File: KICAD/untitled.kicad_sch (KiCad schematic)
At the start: 73 parts, among them IC1 TPA3116D2QDADRQ1, IC2 TPA3116D2QDADRQ1

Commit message: clear
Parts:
- IC1, IC2: footprint TPA3116D2QDADRQ1:SOP65P810X120-33N -> footprints:TPA3116D2QDADRQ1
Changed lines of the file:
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@@
 			)
 		)
-		(property "Footprint" "TPA3116D2QDADRQ1:SOP65P810X120-33N"
+		(property "Footprint" "footprints:TPA3116D2QDADRQ1"
 			(at 177.8 157.15 0)
 			(hide yes)
@@
 			)
 		)
-		(property "Footprint" "TPA3116D2QDADRQ1:SOP65P810X120-33N"
+		(property "Footprint" "footprints:TPA3116D2QDADRQ1"
 			(at 177.8 244.78 0)
 			(hide yes)

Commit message: tiens mec
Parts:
- added R28, R33: 12k, symbol Device:R_Small
- added R32, R34: 13k, symbol Device:R_Small
- added U5, U6: LM321, Package_TO_SOT_SMD:SOT-23-5, symbol Amplifier_Operational:LM321
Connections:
- net GND: now also R28.1, R33.1, U5.2 (V-), U6.2 (V-)
- net at C8.2, IC1.7 (GVDD), R3.1: no longer IC1.6 (PLIMIT)
- net at C30.2, IC2.7 (GVDD), R10.1: no longer IC2.6 (PLIMIT)
- new net: R33.2, R34.2, U6.3 (-)
- new net: R28.2, R32.2, U5.3 (-)
- new net +20V: U5.5 (V+), U6.5 (V+)
- new net AOP_STEREO: U5.1 (+)
- new net AOP_SUB: U6.1 (+)
- new net PLIMIT_STEREO: IC1.6 (PLIMIT), R32.1, U5.4
- new net PLIMIT_SUB: IC2.6 (PLIMIT), R34.1, U6.4

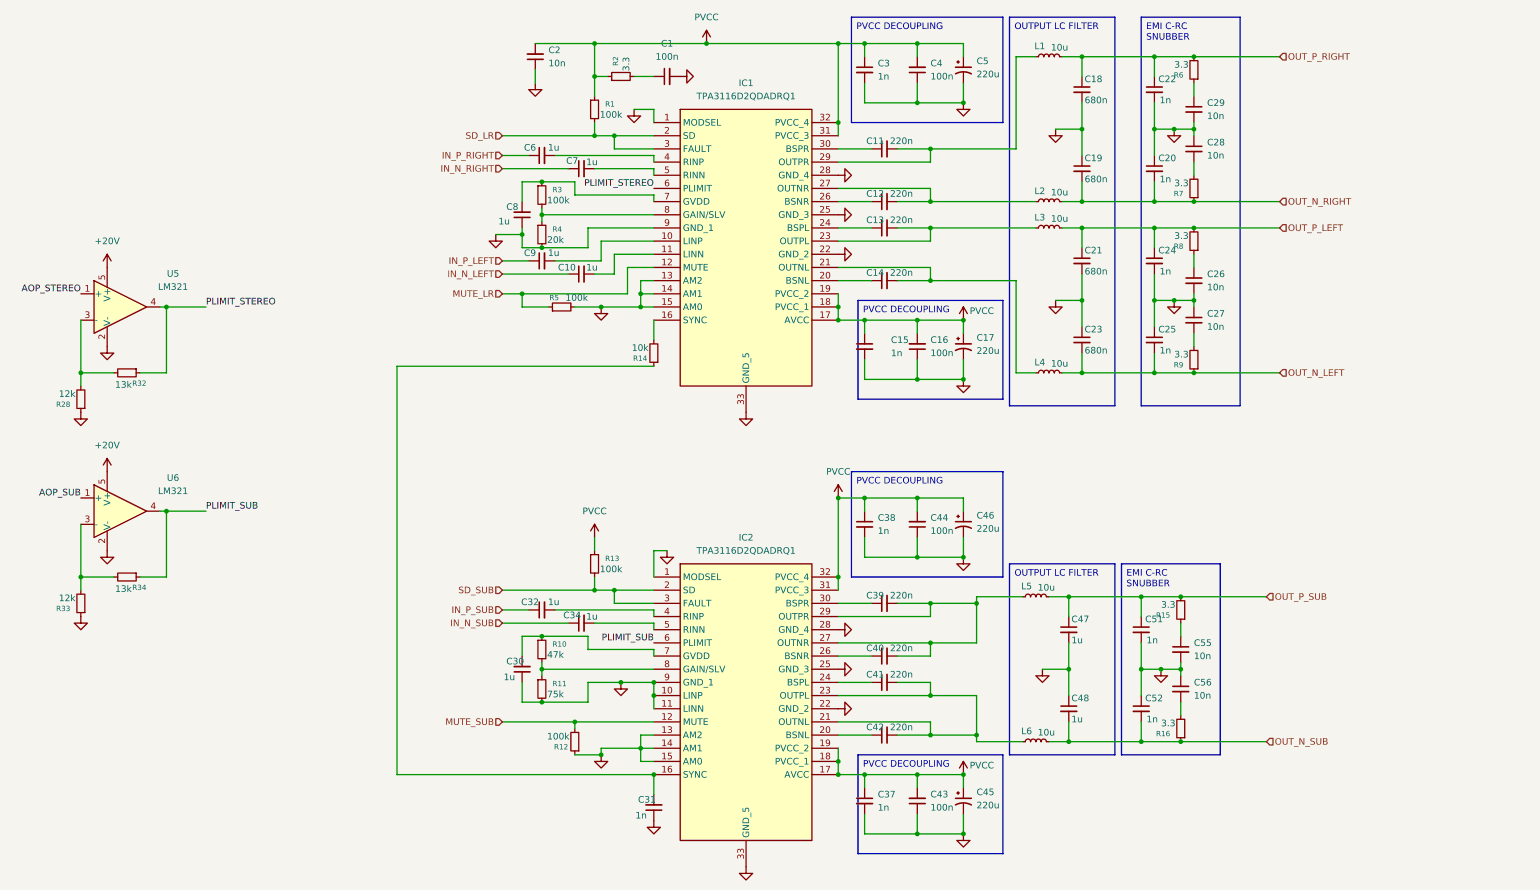
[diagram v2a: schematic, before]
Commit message: supression du subwoofer
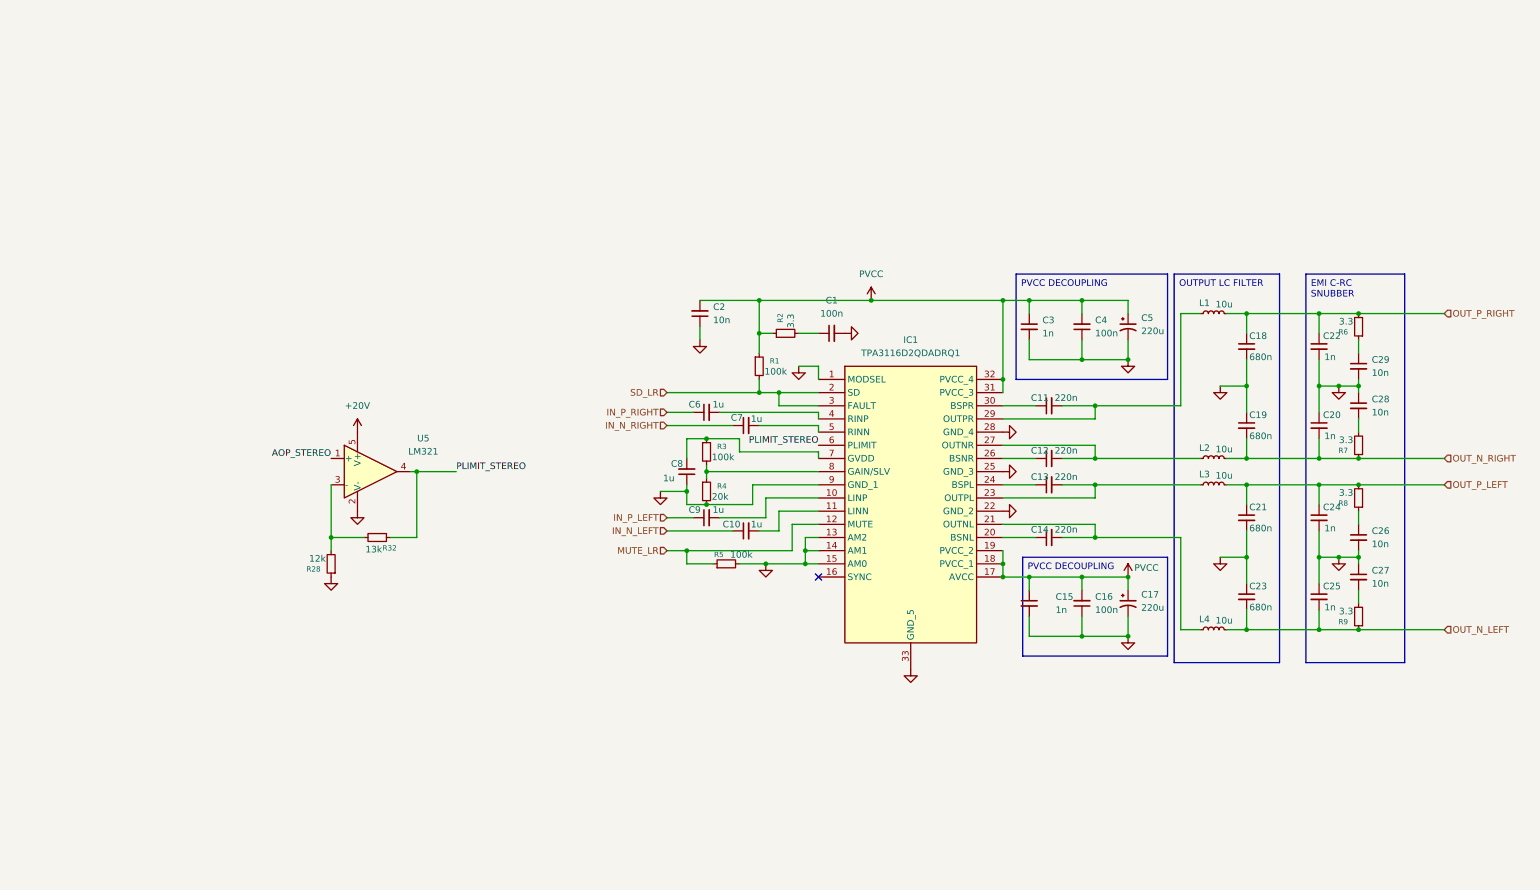
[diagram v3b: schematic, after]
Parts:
- removed C30, C32, C34, C47, C48: 1u, symbol Device:C_Small
- removed C31, C37, C38, C51, C52: 1n, symbol Device:C_Small
- removed C39, C40, C41, C42: 220n, symbol Device:C_Small
- removed C43, C44: 100n, symbol Device:C_Small
- removed C45, C46: 220u, symbol Device:C_Polarized_Small_US
- removed C55, C56: 10n, symbol Device:C_Small
- removed IC2: TPA3116D2QDADRQ1, footprints:TPA3116D2QDADRQ1, symbol TPA3116D2QDADRQ1:TPA3116D2QDADRQ1
- removed L5, L6: 10u, symbol Device:L_Small
- removed R10: 47k, symbol Device:R_Small
- removed R11: 75k, symbol Device:R_Small
- removed R12, R13: 100k, symbol Device:R_Small
- removed R14: 10k, symbol Device:R_Small
- removed R15, R16: 3.3, symbol Device:R_Small
- removed R33: 12k, symbol Device:R_Small
- removed R34: 13k, symbol Device:R_Small
- removed U6: LM321, Package_TO_SOT_SMD:SOT-23-5, symbol Amplifier_Operational:LM321
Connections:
- no-connect marks 0 -> 1
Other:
- moved on the sheet: C1, C10, C11, C12, C13, C14, C15, C16, C17, C18, C19, C2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

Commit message: mise en forme globale
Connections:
- net IN_N_LEFT is gone; now on net GND: C10.1
- net IN_N_RIGHT is gone; now on net GND: C7.1
- net PVCC is gone; now on net Vin: C15.1, C16.2, C17.1, C2.2, C3.1, C4.2, C5.1, IC1.17 (AVCC), IC1.18 (PVCC_1), IC1.19 (PVCC_2), IC1.31 (PVCC_3), IC1.32 (PVCC_4), R1.1, R2.1
- net +20V renamed Vin
- net AOP_STEREO renamed PLIMIT
- net IN_P_LEFT renamed SPK_L
- net IN_P_RIGHT renamed SPK_R
- net MUTE_LR renamed AMP_MUTE
- net SD_LR renamed AMP_SD
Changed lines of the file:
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@@
 	(wire
 		(pts
+			(xy 81.28 127) (xy 83.82 127)
+		)
+		(stroke
+			(width 0)
+			(type default)
+		)
+	)
+	(wire
+		(pts
 			(xy 281.94 119.38) (xy 281.94 121.92)
 		)
@@
 	(wire
 		(pts
+			(xy 165.1 124.46) (xy 177.8 124.46)
+		)
+		(stroke
+			(width 0)
+			(type default)
+		)
+	)
+	(wire
+		(pts
 			(xy 156.21 123.19) (xy 162.56 123.19)
 		)
@@
 		)
 	)
-	(label "AOP_STEREO"
-		(at 83.82 127 180)
-		(effects
-			(font
-				(size 1.27 1.27)
-			)
-			(justify right bottom)
-		)
-	)
 	(label "PLIMIT_STEREO"
-		(at 177.8 124.46 180)
+		(at 165.1 124.46 0)
 		(effects
 			(font
 				(size 1.27 1.27)
 			)
-			(justify right bottom)
+			(justify left bottom)
 		)
 	)
@@
 		)
 	)
-	(hierarchical_label "SD_LR"
+	(hierarchical_label "AMP_SD"
 		(shape input)
 		(at 148.59 114.3 180)
@@
 		)
 	)
-	(hierarchical_label "IN_P_LEFT"
+	(hierarchical_label "SPK_L"
 		(shape input)
 		(at 148.59 138.43 180)
@@
 		)
 	)
-	(hierarchical_label "MUTE_LR"
+	(hierarchical_label "AMP_MUTE"
 		(shape input)
 		(at 148.59 144.78 180)
@@
 		)
 	)
-	(hierarchical_label "IN_P_RIGHT"
+	(hierarchical_label "SPK_R"
 		(shape input)
 		(at 148.59 118.11 180)
@@
 		)
 	)
-	(hierarchical_label "IN_N_LEFT"
-		(shape input)
-		(at 148.59 140.97 180)
-		(effects
-			(font
-				(size 1.27 1.27)
-			)
-			(justify right)
-		)
-	)
 	(hierarchical_label "OUT_P_RIGHT"
 		(shape input)
@@
 		)
 	)
-	(hierarchical_label "IN_N_RIGHT"
+	(hierarchical_label "PLIMIT"
 		(shape input)
-		(at 148.59 120.65 180)
+		(at 81.28 127 180)
 		(effects
 			(font
@@
 			)
 		)
-		(property "Value" "PVCC"
-			(at 187.96 91.44 0)
+		(property "Value" "Vin"
+			(at 190.5 95.2499 0)
 			(show_name no)
 			(do_not_autoplace no)
@@
 					(size 1.27 1.27)
 				)
+				(justify left)
 			)
 		)
@@
 			)
 		)
-		(property "Value" "PVCC"
+		(property "Value" "Vin"
 			(at 241.046 148.082 0)
 			(show_name no)
@@
 	)
 	(symbol
+		(lib_id "power:GND")
+		(at 148.59 120.65 0)
+		(unit 1)
+		(body_style 1)
+		(exclude_from_sim no)
+		(in_bom yes)
+		(on_board yes)
+		(in_pos_files yes)
+		(dnp no)
+		(fields_autoplaced yes)
+		(property "Reference" "#PWR018"
+			(at 148.59 127 0)
+			(hide yes)
+			(show_name no)
+			(do_not_autoplace no)
+			(effects
+				(font
+					(size 1.27 1.27)
+				)
+			)
+		)
+		(property "Value" "GND"
+			(at 148.59 125.73 0)
+			(hide yes)
+			(show_name no)
+			(do_not_autoplace no)
+			(effects
+				(font
+					(size 1.27 1.27)
+				)
+			)
+		)
+		(property "Footprint" ""
+			(at 148.59 120.65 0)
+			(hide yes)
+			(show_name no)
+			(do_not_autoplace no)
+			(effects
+				(font
+					(size 1.27 1.27)
+				)
+			)
+		)
+		(property "Datasheet" ""
+			(at 148.59 120.65 0)
+			(hide yes)
+			(show_name no)
+			(do_not_autoplace no)
+			(effects
+				(font
+					(size 1.27 1.27)
+				)
+			)
+		)
+		(property "Description" "Power symbol creates a global label with name \"GND\" , ground"
+			(at 148.59 120.65 0)
+			(hide yes)
+			(show_name no)
+			(do_not_autoplace no)
+			(effects
+				(font
+					(size 1.27 1.27)
+				)
+			)
+		)
+		(pin "1"
+		)
+		(instances
+			(project "projet_2A"
+				(path "/05601714-c31e-4eda-914b-0c4b098c219a/d2c03650-eb6b-438f-8291-6b9088b7ba31"
+					(reference "#PWR018")
+					(unit 1)
+				)
+			)
+		)
+	)
+	(symbol
 		(lib_id "Device:R_Small")
 		(at 156.21 133.35 0)
@@
 			)
 		)
-		(property "Value" "+20V"
-			(at 88.9 116.84 0)
+		(property "Value" "Vin"
+			(at 91.44 120.6499 0)
 			(show_name no)
 			(do_not_autoplace no)
@@
 					(size 1.27 1.27)
 				)
+				(justify left)
 			)
 		)
@@
 					(unit 1)
 				)
+			)
+		)
+	)
+	(symbol
+		(lib_id "power:GND")
+		(at 148.59 140.97 0)
+		(unit 1)
+		(body_style 1)
+		(exclude_from_sim no)
+		(in_bom yes)
+		(on_board yes)
+		(in_pos_files yes)
+		(dnp no)
+		(fields_autoplaced yes)
+		(property "Reference" "#PWR019"
+			(at 148.59 147.32 0)
+			(hide yes)
+			(show_name no)
+			(do_not_autoplace no)
+			(effects
+				(font
+					(size 1.27 1.27)
+				)
+			)
+		)
+		(property "Value" "GND"
+			(at 148.59 146.05 0)
+			(hide yes)
+			(show_name no)
+			(do_not_autoplace no)
+			(effects
+				(font
+					(size 1.27 1.27)
+				)
+			)
+		)
+		(property "Footprint" ""
+			(at 148.59 140.97 0)
+			(hide yes)
+			(show_name no)
+			(do_not_autoplace no)
+			(effects
+				(font
+					(size 1.27 1.27)
+				)
+			)
+		)
+		(property "Datasheet" ""
+			(at 148.59 140.97 0)
+			(hide yes)
+			(show_name no)
+			(do_not_autoplace no)
+			(effects
+				(font
+					(size 1.27 1.27)
+				)
+			)
+		)
+		(property "Description" "Power symbol creates a global label with name \"GND\" , ground"
+			(at 148.59 140.97 0)
+			(hide yes)
+			(show_name no)
+			(do_not_autoplace no)
+			(effects
+				(font
+					(size 1.27 1.27)
+				)
+			)
+		)
+		(pin "1"
+		)
+		(instances
+			(project "projet_2A"
+				(path "/05601714-c31e-4eda-914b-0c4b098c219a/d2c03650-eb6b-438f-8291-6b9088b7ba31"
+					(reference "#PWR019")
+					(unit 1)
+				)

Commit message: interface HM
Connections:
- net PLIMIT renamed AMP_PLIMIT
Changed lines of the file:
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@@
 		)
 	)
-	(hierarchical_label "PLIMIT"
+	(hierarchical_label "AMP_PLIMIT"
 		(shape input)
 		(at 81.28 127 180)
